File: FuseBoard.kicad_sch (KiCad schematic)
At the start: 22 parts, among them J1 Conn_01x02_Socket, J10 Conn_01x02_Socket, J2 Conn_01x02_Socket, J3 Conn_01x02_Socket, J4 Conn_01x02_Socket, J5 Conn_01x02_Socket, J6 Conn_01x02_Socket, J7 Conn_01x02_Socket, J8 Conn_01x02_Socket, J9 Conn_01x02_Socket

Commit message: changes to pcb
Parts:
- added J11: Conn_01x02_Socket, Connector_AMASS:AMASS_XT30PW-M_1x02_P2.50mm_Horizontal, symbol Connector:Conn_01x02_Socket
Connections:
- net GND: now reaches J1.1 (Pin_1), J2.1 (Pin_1), J3.1 (Pin_1), J4.1 (Pin_1), U1. (OUT-)
- net GND: now also J5.1 (Pin_1), J6.1 (Pin_1), J7.1 (Pin_1), J8.1 (Pin_1), J9.1 (Pin_1), U2. (OUT-)
- net at J10.1 (Pin_1), U3. (OUT-): now also J11.1 (Pin_1)
- new net: J11.2 (Pin_2), U3. (OUT-)
- new net: J9.2 (Pin_2), U1. (OUT-), U2. (OUT-)
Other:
- moved on the sheet: U1, U2, U3

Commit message: updated pcb
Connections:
- net +12V: now reaches F4.3, F4.4, F6.3, F6.4, F7.3, F7.4, F8.3, F8.4, U2. (OUT-)
- net +5V: now reaches F1.3, F1.4, F2.3, F2.4, F3.3, F3.4, F5.3, F5.4, U1. (OUT-)
- new net: J9.2 (Pin_2), U1. (OUT-), U2. (OUT-)
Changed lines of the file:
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@@
+	)
+	(junction
+		(at 209.55 76.2)
+		(diameter 0)
+		(color 0 0 0 0)
+	)
+	(junction
+		(at 132.08 76.2)
+		(diameter 0)
+		(color 0 0 0 0)
 	)
 	(junction
@@
 	(wire
 		(pts
-			(xy 201.93 76.2) (xy 218.44 76.2)
+			(xy 201.93 76.2) (xy 209.55 76.2)
 		)
 		(stroke
@@
 	(wire
 		(pts
+			(xy 209.55 76.2) (xy 218.44 76.2)
+		)
+		(stroke
+			(width 0)
+			(type default)
+		)
+	)
+	(wire
+		(pts
 			(xy 185.42 119.38) (xy 185.42 120.65)
 		)
@@
 	(wire
 		(pts
+			(xy 132.08 76.2) (xy 138.43 76.2)
+		)
+		(stroke
+			(width 0)
+			(type default)
+		)
+	)
+	(wire
+		(pts
 			(xy 140.97 76.2) (xy 157.48 76.2)
 		)
@@
 	(wire
 		(pts
-			(xy 121.92 76.2) (xy 138.43 76.2)
+			(xy 121.92 76.2) (xy 132.08 76.2)
 		)
 		(stroke
@@
 	)
 	(symbol
+		(lib_id "power:+12V")
+		(at 209.55 76.2 0)
+		(unit 1)
+		(exclude_from_sim no)
+		(in_bom yes)
+		(on_board yes)
+		(dnp no)
+		(fields_autoplaced yes)
+		(property "Reference" "#PWR2"
+			(at 209.55 80.01 0)
+			(effects
+				(font
+					(size 1.27 1.27)
+				)
+				(hide yes)
+			)
+		)
+		(property "Value" "+12V"
+			(at 209.55 71.12 0)
+			(effects
+				(font
+					(size 1.27 1.27)
+				)
+			)
+		)
+		(property "Footprint" ""
+			(at 209.55 76.2 0)
+			(effects
+				(font
+					(size 1.27 1.27)
+				)
+				(hide yes)
+			)
+		)
+		(property "Datasheet" ""
+			(at 209.55 76.2 0)
+			(effects
+				(font
+					(size 1.27 1.27)
+				)
+				(hide yes)
+			)
+		)
+		(property "Description" "Power symbol creates a global label with name \"+12V\""
+			(at 209.55 76.2 0)
+			(effects
+				(font
+					(size 1.27 1.27)
+				)
+				(hide yes)
+			)
+		)
+		(pin "1"
+		)
+		(instances
+			(project ""
+				(path "/871f4914-5702-497a-825f-1dde939a79f8"
+					(reference "#PWR2")
+					(unit 1)
+				)
+			)
+		)
+	)
+	(symbol
 		(lib_id "Connector:Conn_01x02_Socket")
 		(at 242.57 125.73 270)
@@
 					(unit 1)
 				)
+			)
+		)
+	)
+	(symbol
+		(lib_id "power:+5V")
+		(at 132.08 76.2 0)
+		(unit 1)
+		(exclude_from_sim no)
+		(in_bom yes)
+		(on_board yes)
+		(dnp no)
+		(fields_autoplaced yes)
+		(property "Reference" "#PWR3"
+			(at 132.08 80.01 0)
+			(effects
+				(font
+					(size 1.27 1.27)
+				)
+				(hide yes)
+			)
+		)
+		(property "Value" "+5V"
+			(at 132.08 71.12 0)
+			(effects
+				(font
+					(size 1.27 1.27)
+				)
+			)
+		)
+		(property "Footprint" ""
+			(at 132.08 76.2 0)
+			(effects
+				(font
+					(size 1.27 1.27)
+				)
+				(hide yes)
+			)
+		)
+		(property "Datasheet" ""
+			(at 132.08 76.2 0)
+			(effects
+				(font
+					(size 1.27 1.27)
+				)
+				(hide yes)
+			)
+		)
+		(property "Description" "Power symbol creates a global label with name \"+5V\""
+			(at 132.08 76.2 0)
+			(effects
+				(font
+					(size 1.27 1.27)
+				)
+				(hide yes)
+			)
+		)
+		(pin "1"
+		)
+		(instances
+			(project ""
+				(path "/871f4914-5702-497a-825f-1dde939a79f8"
+					(reference "#PWR3")
+					(unit 1)
+				)

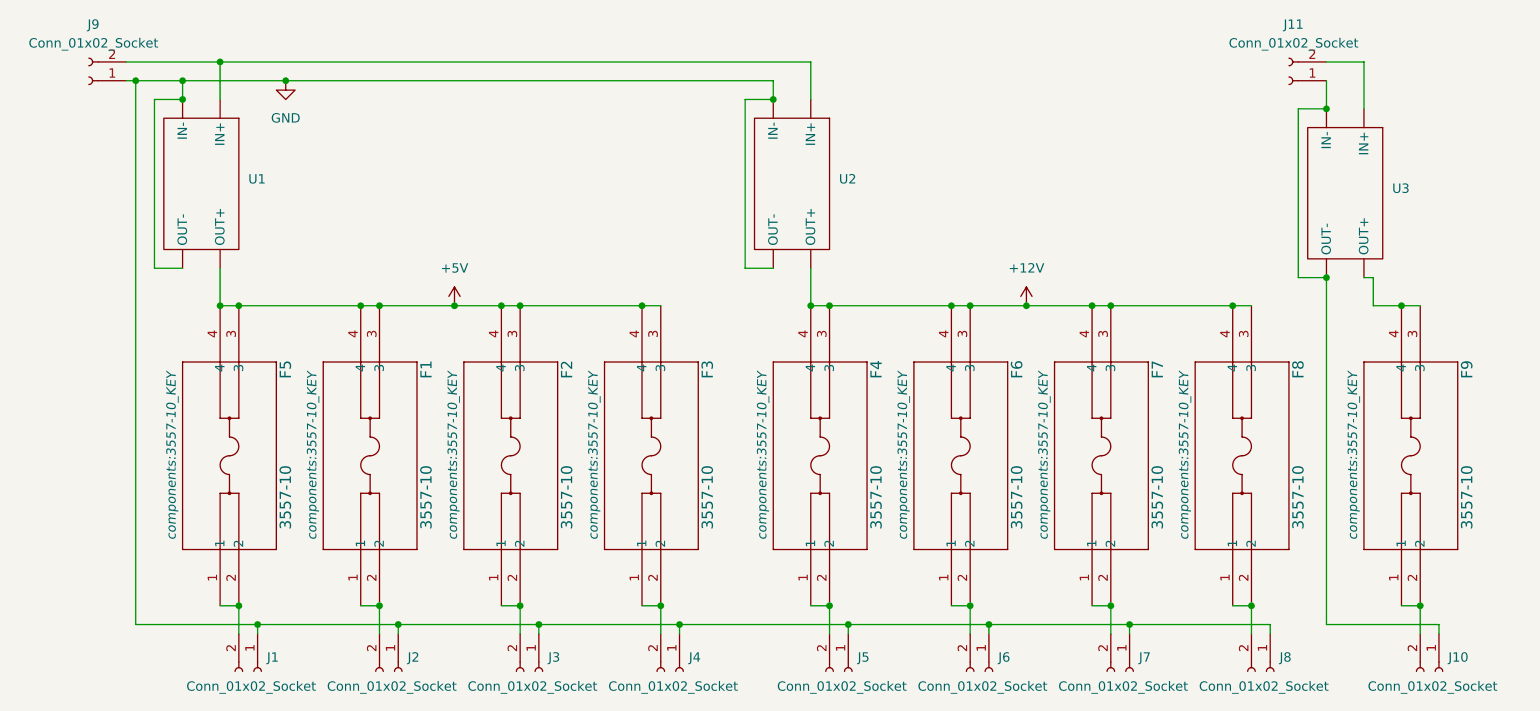
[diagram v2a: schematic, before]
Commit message: separated GNDs
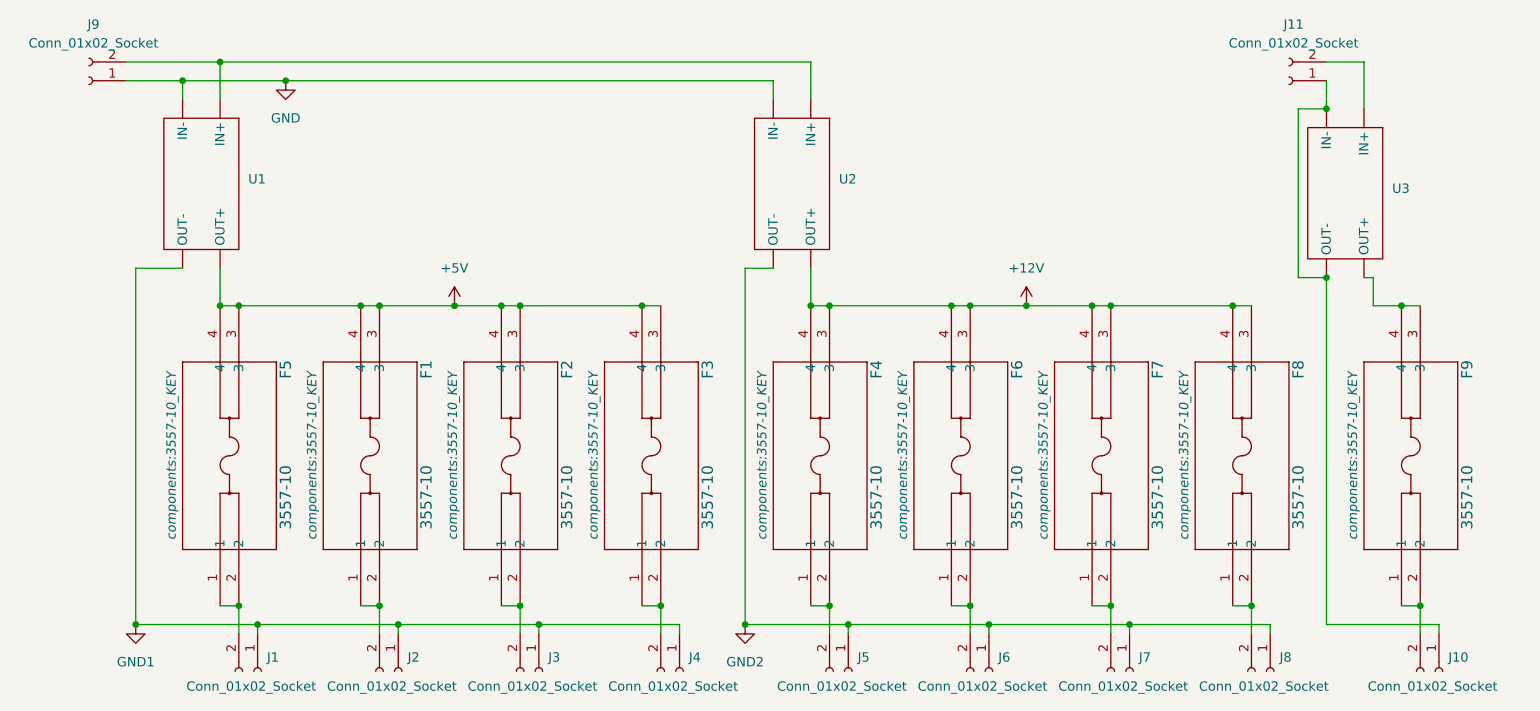
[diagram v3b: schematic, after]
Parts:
- J11, J9: footprint Connector_AMASS:AMASS_XT30PW-M_1x02_P2.50mm_Horizontal -> Connector_AMASS:AMASS_XT30PW-F_1x02_P2.50mm_Horizontal
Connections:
- net GND: no longer J1.1 (Pin_1), J2.1 (Pin_1), J3.1 (Pin_1), J4.1 (Pin_1), J5.1 (Pin_1), J6.1 (Pin_1), J7.1 (Pin_1), J8.1 (Pin_1)
- new net: J9.2 (Pin_2), U1. (OUT-), U2. (OUT-)
- new net GND1: J1.1 (Pin_1), J2.1 (Pin_1), J3.1 (Pin_1), J4.1 (Pin_1), U1. (OUT-)
- new net GND2: J5.1 (Pin_1), J6.1 (Pin_1), J7.1 (Pin_1), J8.1 (Pin_1), U2. (OUT-)
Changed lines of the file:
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@@
 (kicad_sch
-	(version 20231120)
+	(version 20250114)
 	(generator "eeschema")
-	(generator_version "8.0")
+	(generator_version "9.0")
 	(paper "A4")
 	(junction
@@
 	)
 	(junction
+		(at 185.42 119.38)
+		(diameter 0)
+		(color 0 0 0 0)
+	)
+	(junction
 		(at 182.88 76.2)
 		(diameter 0)
@@
 	)
 	(junction
-		(at 162.56 119.38)
-		(diameter 0)
-		(color 0 0 0 0)
-	)
-	(junction
 		(at 140.97 116.84)
 		(diameter 0)
@@
 	)
 	(junction
-		(at 175.26 48.26)
-		(diameter 0)
-		(color 0 0 0 0)
-	)
-	(junction
 		(at 180.34 76.2)
 		(diameter 0)
@@
 	)
 	(junction
-		(at 185.42 119.38)
-		(diameter 0)
-		(color 0 0 0 0)
-	)
-	(junction
 		(at 201.93 116.84)
 		(diameter 0)
@@
 	)
 	(junction
-		(at 95.25 48.26)
-		(diameter 0)
-		(color 0 0 0 0)
-	)
-	(junction
 		(at 109.22 45.72)
 		(diameter 0)
@@
 	)
 	(junction
+		(at 88.9 119.38)
+		(diameter 0)
+		(color 0 0 0 0)
+	)
+	(junction
+		(at 171.45 119.38)
+		(diameter 0)
+		(color 0 0 0 0)
+	)
+	(junction
 		(at 250.19 49.53)
 		(diameter 0)
@@
 	)
 	(junction
-		(at 88.9 45.72)
-		(diameter 0)
-		(color 0 0 0 0)
-	)
-	(junction
 		(at 237.49 76.2)
 		(diameter 0)
@@
 	(wire
 		(pts
-			(xy 88.9 45.72) (xy 88.9 119.38)
-		)
-		(stroke
-			(width 0)
-			(type default)
-		)
-	)
-	(wire
-		(pts
 			(xy 201.93 76.2) (xy 209.55 76.2)
 		)
@@
 	(wire
 		(pts
-			(xy 171.45 48.26) (xy 175.26 48.26)
-		)
-		(stroke
-			(width 0)
-			(type default)
-		)
-	)
-	(wire
-		(pts
 			(xy 180.34 116.84) (xy 182.88 116.84)
 		)
@@
 	(wire
 		(pts
+			(xy 171.45 71.12) (xy 171.45 119.38)
+		)
+		(stroke
+			(width 0)
+			(type default)
+		)
+	)
+	(wire
+		(pts
 			(xy 199.39 116.84) (xy 201.93 116.84)
 		)
@@
 	(wire
 		(pts
-			(xy 171.45 71.12) (xy 171.45 48.26)
-		)
-		(stroke
-			(width 0)
-			(type default)
-		)
-	)
-	(wire
-		(pts
 			(xy 204.47 119.38) (xy 223.52 119.38)
 		)
@@
 	(wire
 		(pts
-			(xy 95.25 71.12) (xy 91.44 71.12)
-		)
-		(stroke
-			(width 0)
-			(type default)
-		)
-	)
-	(wire
-		(pts
 			(xy 100.33 76.2) (xy 102.87 76.2)
 		)
@@
 	(wire
 		(pts
-			(xy 91.44 71.12) (xy 91.44 48.26)
-		)
-		(stroke
-			(width 0)
-			(type default)
-		)
-	)
-	(wire
-		(pts
-			(xy 91.44 48.26) (xy 95.25 48.26)
+			(xy 171.45 119.38) (xy 185.42 119.38)
 		)
 		(stroke
@@
 	(wire
 		(pts
-			(xy 88.9 45.72) (xy 95.25 45.72)
-		)
-		(stroke
-			(width 0)
-			(type default)
-		)
-	)
-	(wire
-		(pts
 			(xy 180.34 48.26) (xy 180.34 43.18)
 		)
@@
 	(wire
 		(pts
-			(xy 162.56 119.38) (xy 185.42 119.38)
-		)
-		(stroke
-			(width 0)
-			(type default)
-		)
-	)
-	(wire
-		(pts
 			(xy 160.02 116.84) (xy 160.02 120.65)
 		)
@@
 	(wire
 		(pts
+			(xy 88.9 119.38) (xy 88.9 71.12)
+		)
+		(stroke
+			(width 0)
+			(type default)
+		)
+	)
+	(wire
+		(pts
 			(xy 121.92 76.2) (xy 132.08 76.2)
 		)
@@
 	(wire
 		(pts
+			(xy 88.9 71.12) (xy 95.25 71.12)
+		)
+		(stroke
+			(width 0)
+			(type default)
+		)
+	)
+	(wire
+		(pts
 			(xy 109.22 45.72) (xy 175.26 45.72)
 		)
@@
 	(wire
 		(pts
-			(xy 87.63 45.72) (xy 88.9 45.72)
+			(xy 87.63 45.72) (xy 95.25 45.72)
 		)
 		(stroke
@@
 			)
 		)
-		(property "Footprint" "Connector_AMASS:AMASS_XT30PW-M_1x02_P2.50mm_Horizontal"
+		(property "Footprint" "Connector_AMASS:AMASS_XT30PW-F_1x02_P2.50mm_Horizontal"
 			(at 245.11 45.72 0)
 			(effects
@@
 	)
 	(symbol
+		(lib_id "power:GND2")
+		(at 171.45 119.38 0)
+		(unit 1)
+		(exclude_from_sim no)
+		(in_bom yes)
+		(on_board yes)
+		(dnp no)
+		(fields_autoplaced yes)
+		(property "Reference" "#PWR05"
+			(at 171.45 125.73 0)
+			(effects
+				(font
+					(size 1.27 1.27)
+				)
+				(hide yes)
+			)
+		)
+		(property "Value" "GND2"
+			(at 171.45 124.46 0)
+			(effects
+				(font
+					(size 1.27 1.27)
+				)
+			)
+		)
+		(property "Footprint" ""
+			(at 171.45 119.38 0)
+			(effects
+				(font
+					(size 1.27 1.27)
+				)
+				(hide yes)
+			)
+		)
+		(property "Datasheet" ""
+			(at 171.45 119.38 0)
+			(effects
+				(font
+					(size 1.27 1.27)
+				)
+				(hide yes)
+			)
+		)
+		(property "Description" "Power symbol creates a global label with name \"GND2\" , ground"
+			(at 171.45 119.38 0)
+			(effects
+				(font
+					(size 1.27 1.27)
+				)
+				(hide yes)
+			)
+		)
+		(pin "1"
+		)
+		(instances
+			(project ""
+				(path "/871f4914-5702-497a-825f-1dde939a79f8"
+					(reference "#PWR05")
+					(unit 1)
+				)
+			)
+		)
+	)
+	(symbol
 		(lib_id "power:+12V")
 		(at 209.55 76.2 0)
@@
 			)
 		)
-		(property "Footprint" "Connector_AMASS:AMASS_XT30PW-M_1x02_P2.50mm_Horizontal"
+		(property "Footprint" "Connector_AMASS:AMASS_XT30PW-F_1x02_P2.50mm_Horizontal"
 			(at 82.55 45.72 0)
 			(effects
@@
 	)
 	(symbol
+		(lib_id "power:GND1")
+		(at 88.9 119.38 0)
+		(unit 1)
+		(exclude_from_sim no)
+		(in_bom yes)
+		(on_board yes)
+		(dnp no)
+		(fields_autoplaced yes)
+		(property "Reference" "#PWR04"
+			(at 88.9 125.73 0)
+			(effects
+				(font
+					(size 1.27 1.27)
+				)
+				(hide yes)
+			)
+		)
+		(property "Value" "GND1"
+			(at 88.9 124.46 0)
+			(effects
+				(font
+					(size 1.27 1.27)
+				)
+			)
+		)
+		(property "Footprint" ""
+			(at 88.9 119.38 0)
+			(effects
+				(font
+					(size 1.27 1.27)
+				)
+				(hide yes)
+			)
+		)
+		(property "Datasheet" ""
+			(at 88.9 119.38 0)
+			(effects
+				(font
+					(size 1.27 1.27)
+				)
+				(hide yes)
+			)
+		)
+		(property "Description" "Power symbol creates a global label with name \"GND1\" , ground"
+			(at 88.9 119.38 0)
+			(effects
+				(font
+					(size 1.27 1.27)
+				)
+				(hide yes)
+			)
+		)
+		(pin "1"
+		)
+		(instances
+			(project ""
+				(path "/871f4914-5702-497a-825f-1dde939a79f8"
+					(reference "#PWR04")
+					(unit 1)
+				)
+			)
+		)
+	)
+	(symbol
 		(lib_id "Connector:Conn_01x02_Socket")
 		(at 124.46 125.73 270)
@@
 		)
 	)
+	(embedded_fonts no)
 )
